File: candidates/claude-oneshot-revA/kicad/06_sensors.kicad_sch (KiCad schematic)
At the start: 12 parts, among them U30 ICM-42688-P, U31 MMC5983MA, U32 BMP581, U33 SHT40-AD1B-R2

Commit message: docs: show one-shot candidate renders and schematic in README, fix 3D models
Root README gains a status table for the Claude one-shot candidate, 3D and
enclosure renders, PCB copper view, all 12 schematic sheets as images and
step-by-step instructions (folders) to open the KiCad project or the STEP
files. Candidate README gets the same gallery and KiCad instructions.

3D: envelope STEP models for parts whose footprint had no model in the
KiCad 10.0.6 install (MAX-M10S, ICM-42688-P, MMC5983MA, BMP581, TPD1E0B04,
TPS259474L RPW, TUSB320LAI, Coilcraft inductors, SHT40), so the board STEP
and the Alt+3 view are complete. Routing unchanged; DRC 1 reviewed error,
11 unconnected, parity 0.

Co-Authored-By: Claude Opus 5.5 <noreply@anthropic.com>
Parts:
- U33: footprint Sensor_Humidity:Sensirion_DFN-4_1.5x1.5mm_P0.8mm_SHT4x_NoCentralPad -> SC:Sensirion_DFN-4_1.5x1.5mm_P0.8mm_SHT4x_NoCentralPad
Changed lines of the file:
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@@
   (property "Reference" "U33" (at 264.16 45.72 0) (effects (font (size 1.27 1.27)) (justify left)))
   (property "Value" "SHT40-AD1B-R2" (at 264.16 48.26 0) (effects (font (size 1.27 1.27)) (justify left)))
-  (property "Footprint" "Sensor_Humidity:Sensirion_DFN-4_1.5x1.5mm_P0.8mm_SHT4x_NoCentralPad" (at 271.78 57.15 0) (effects (font (size 1.27 1.27)) (hide yes)))
+  (property "Footprint" "SC:Sensirion_DFN-4_1.5x1.5mm_P0.8mm_SHT4x_NoCentralPad" (at 271.78 57.15 0) (effects (font (size 1.27 1.27)) (hide yes)))
   (property "MPN" "SHT40-AD1B-R2" (at 271.78 57.15 0) (effects (font (size 1.27 1.27)) (hide yes)))
   (property "Status" "LOCKED" (at 271.78 57.15 0) (effects (font (size 1.27 1.27)) (hide yes)))

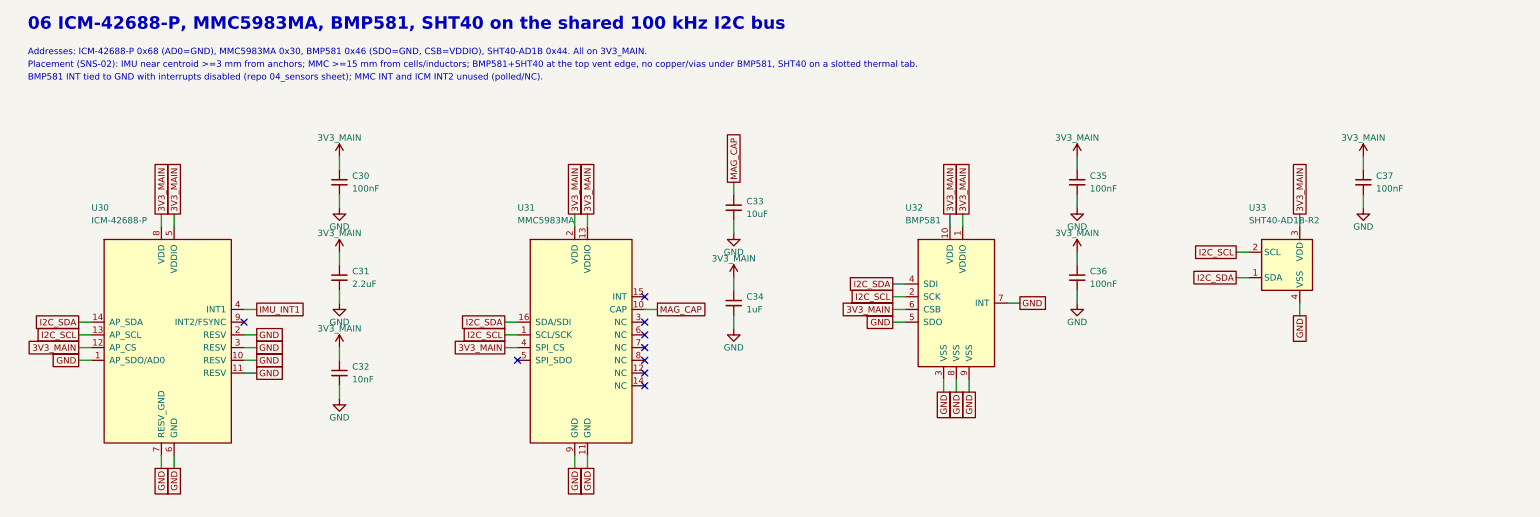
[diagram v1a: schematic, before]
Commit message: candidates: evidence-backed refinement of the Claude one-shot KiCad candidate
Reviewed on origin/main e1f75a3 with KiCad 10.0.6; changes stay inside
candidates/claude-oneshot-revA/ and close no project gate.

- TXU0202 U24: exact TI DCU0008A land (SCES942A pp.32-34) replaces the
  generic KiCad DCU footprint; schematic/symbol footprint fields updated.
- TPS259474L U3 RPW: copper verified against the TI 4225183/A vectors;
  paste now follows the TI stencil example, fab body 2.0 mm.
- ICM-42688-P pin 9 tied to GND (TDK DS-000347 v1.9 Table 10).
- U1/J5 body-courtyard overlap fixed, duplicate vias removed, BMP581
  under-body SCL route removed, SHT40 SDA and 3V3 fragments connected,
  three GND islands stitched, C57 connected, silkscreen refined.
- Removed the unreviewed mask-bridge suppression on U30/U32; findings
  are now visible pending assembler review.
- Before/after ERC, DRC+parity, unconnected and net/pad reconciliation
  reports plus docs/REFINEMENT_2026_09_23.md. Remaining: floating GND at
  U2/U3/U24, SX1262 RF blocker, O05 and the other open gates.

Co-Authored-By: Claude Opus 5.5 <noreply@anthropic.com>
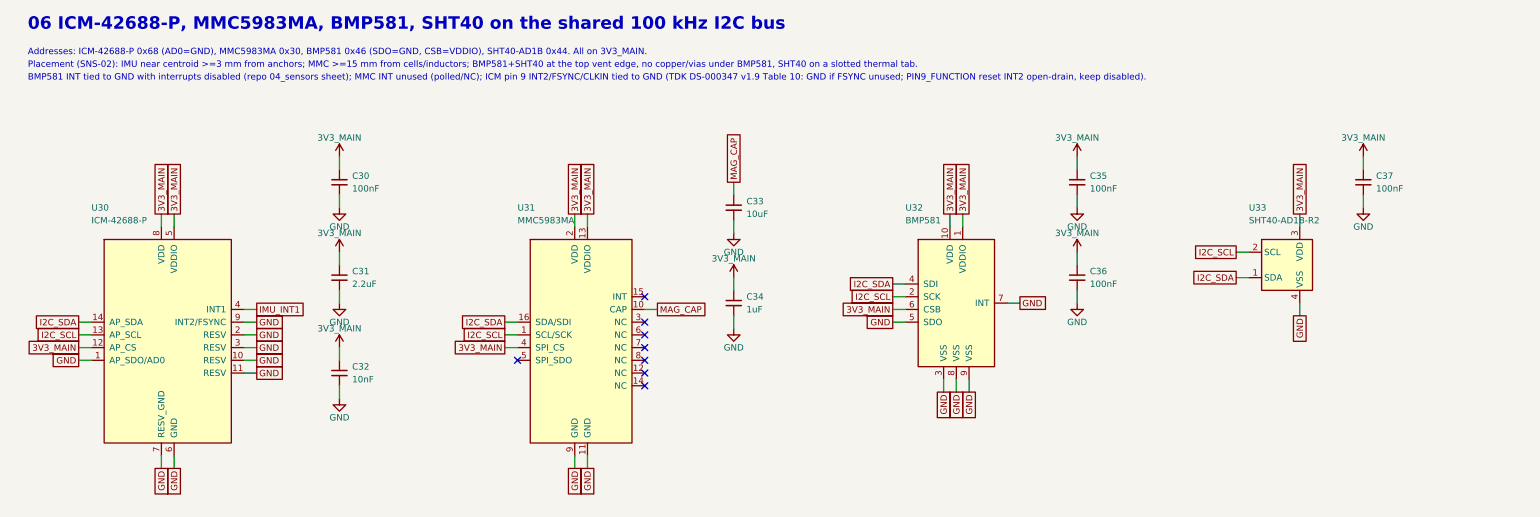
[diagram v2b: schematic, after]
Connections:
- net GND: now also U30.9 (INT2/FSYNC)
- no-connect marks 9 -> 8
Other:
- note added: "BMP581 INT tied to GND with interrupts disabled (repo 04_sensors sheet); MMC INT unused (polled/NC); ICM pin 9 INT2/FSYNC/CLKIN tied to GND (TDK DS-000347 v1.9 Table 10: GND if FSYNC unused; PIN9_FUNCTION reset INT2 open-drain, keep disabled)."
- note removed: "BMP581 INT tied to GND with interrupts disabled (repo 04_sensors sheet); MMC INT and ICM INT2 unused (polled/NC)."
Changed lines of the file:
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@@
   (wire (pts (xy 49.53 95.25) (xy 49.53 97.79)) (stroke (width 0) (type default)))
   (global_label "GND" (shape passive) (at 49.53 97.79 270) (fields_autoplaced yes) (effects (font (size 1.27 1.27)) (justify right)) (property "Intersheetrefs" "${INTERSHEET_REFS}" (at 49.53 97.79 0) (effects (font (size 1.27 1.27)) (hide yes))))
-  (no_connect (at 63.5 68.58))
+  (wire (pts (xy 63.5 68.58) (xy 66.04 68.58)) (stroke (width 0) (type default)))
+  (global_label "GND" (shape passive) (at 66.04 68.58 0) (fields_autoplaced yes) (effects (font (size 1.27 1.27)) (justify left)) (property "Intersheetrefs" "${INTERSHEET_REFS}" (at 66.04 68.58 0) (effects (font (size 1.27 1.27)) (hide yes))))
   (symbol (lib_id "Device:C_Small") (at 82.55 40.64 0) (unit 1)
   (exclude_from_sim no) (in_bom yes) (on_board yes) (dnp no)
@@
   (text "Addresses: ICM-42688-P 0x68 (AD0=GND), MMC5983MA 0x30, BMP581 0x46 (SDO=GND, CSB=VDDIO), SHT40-AD1B 0x44. All on 3V3_MAIN." (exclude_from_sim no) (at 20.32 13.97 0) (effects (font (size 1.27 1.27)) (justify left top)))
   (text "Placement (SNS-02): IMU near centroid >=3 mm from anchors; MMC >=15 mm from cells/inductors; BMP581+SHT40 at the top vent edge, no copper/vias under BMP581, SHT40 on a slotted thermal tab." (exclude_from_sim no) (at 20.32 16.51 0) (effects (font (size 1.27 1.27)) (justify left top)))
-  (text "BMP581 INT tied to GND with interrupts disabled (repo 04_sensors sheet); MMC INT and ICM INT2 unused (polled/NC)." (exclude_from_sim no) (at 20.32 19.05 0) (effects (font (size 1.27 1.27)) (justify left top)))
+  (text "BMP581 INT tied to GND with interrupts disabled (repo 04_sensors sheet); MMC INT unused (polled/NC); ICM pin 9 INT2/FSYNC/CLKIN tied to GND (TDK DS-000347 v1.9 Table 10: GND if FSYNC unused; PIN9_FUNCTION reset INT2 open-drain, keep disabled)." (exclude_from_sim no) (at 20.32 19.05 0) (effects (font (size 1.27 1.27)) (justify left top)))
   (embedded_fonts no)
 )
